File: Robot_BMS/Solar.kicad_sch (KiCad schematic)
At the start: 19 parts, among them J3 691137710002, U5 LM3488MM, U6 CSD18563Q5A

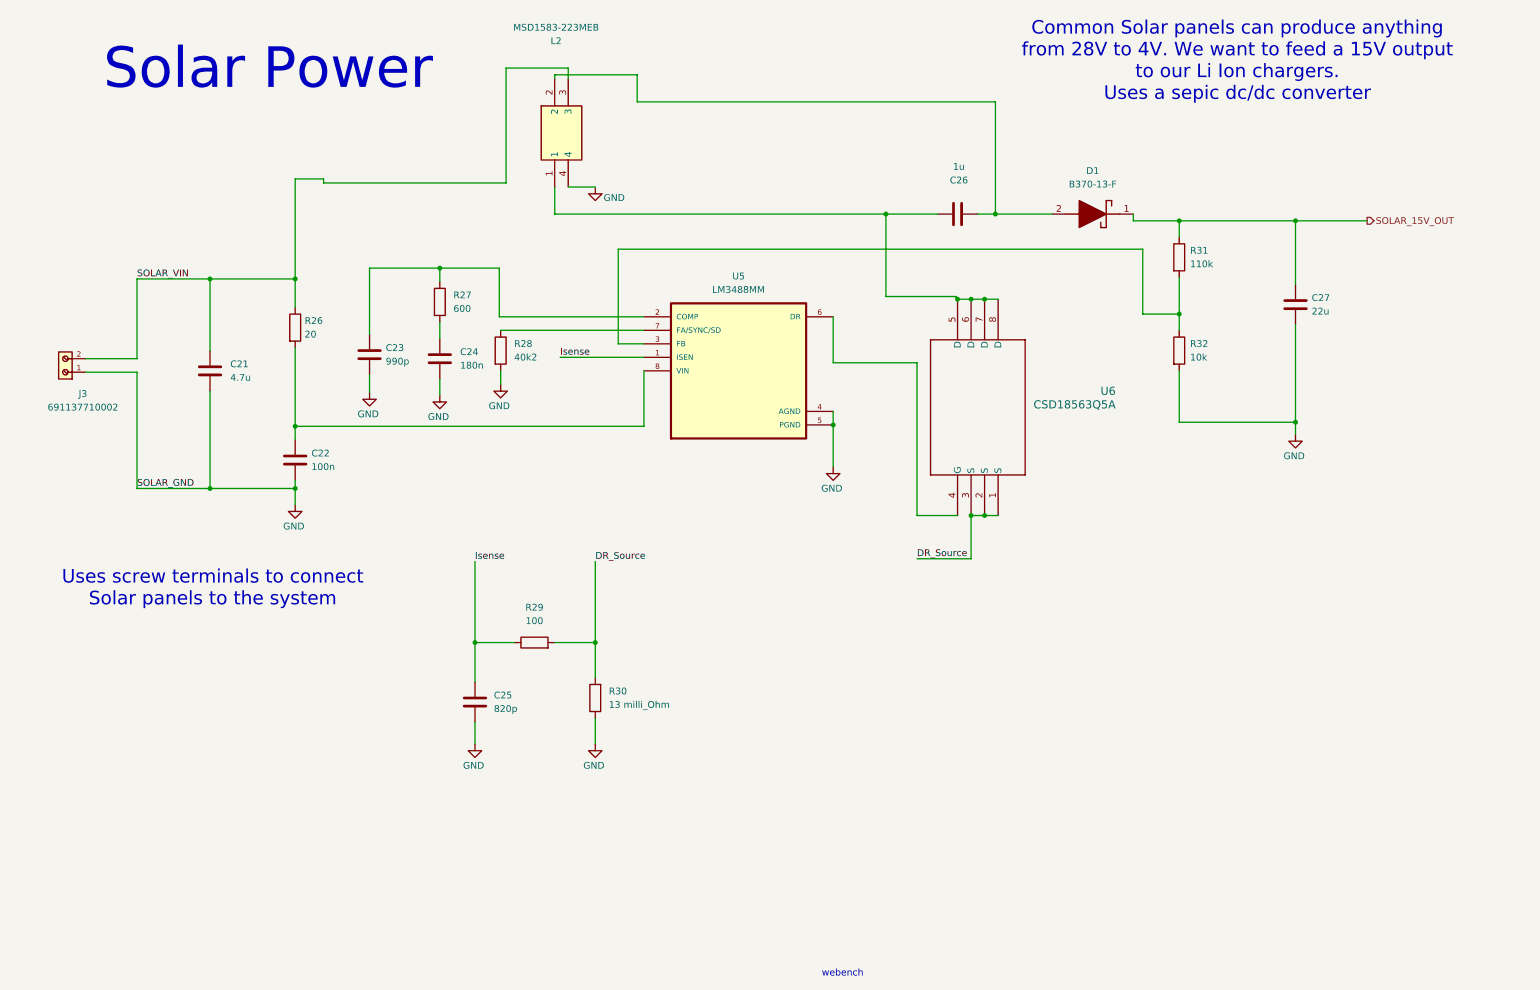
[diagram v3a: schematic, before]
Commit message: System drawing down on top schematic, will start inputting footprints
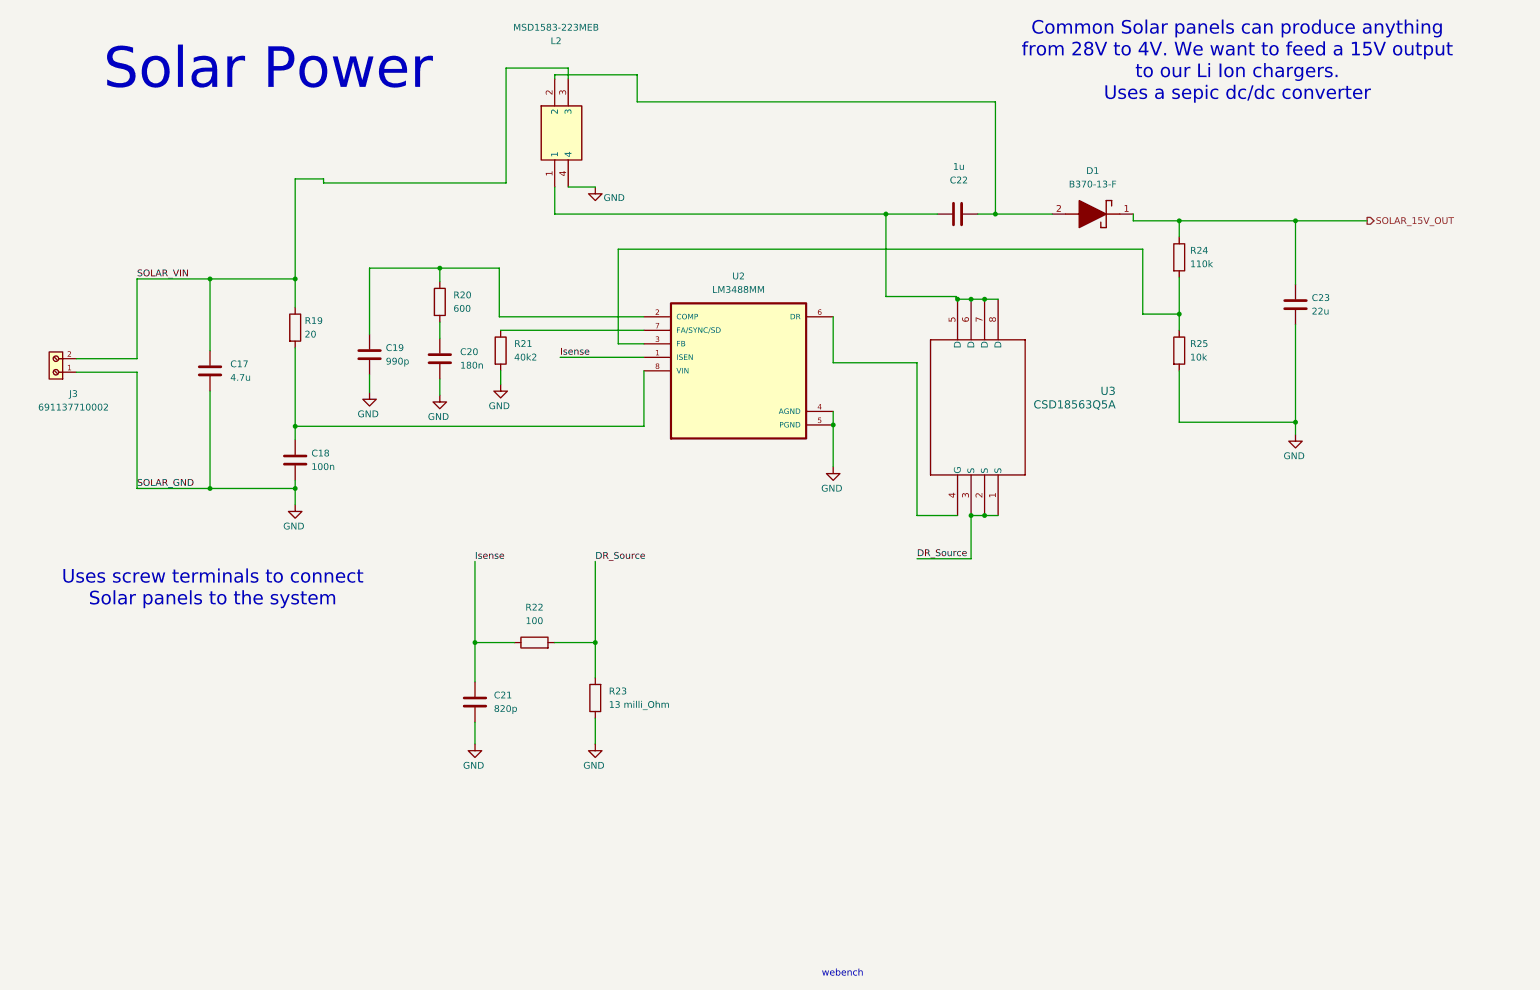
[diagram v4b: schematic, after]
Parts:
- renumbered C21 to C17, C22 to C18, C23 to C19, C24 to C20, C25 to C21, C26 to C22, C27 to C23, R26 to R19, R27 to R20, R28 to R21, R29 to R22, R30 to R23, R31 to R24, R32 to R25, U5 to U2, U6 to U3
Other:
- moved on the sheet: J3
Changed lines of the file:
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@@
 	(wire
 		(pts
-			(xy 21.082 78.994) (xy 30.734 78.994)
+			(xy 19.304 78.994) (xy 30.734 78.994)
 		)
 		(stroke
@@
 	(wire
 		(pts
-			(xy 21.082 81.534) (xy 30.734 81.534)
+			(xy 19.304 81.534) (xy 30.734 81.534)
 		)
 		(stroke
@@
 		(on_board yes)
 		(dnp no)
-		(property "Reference" "#PWR037"
+		(property "Reference" "#PWR030"
 			(at 60.452 112.776 0)
 			(effects
@@
 			(project "Robot_BMS"
 				(path "/72551b1c-3d40-4199-8911-e5b015f4abec/ff8c01d9-7d3c-4161-8f4f-7a8402a9daec"
-					(reference "#PWR037")
+					(reference "#PWR030")
 					(unit 1)
 				)
@@
 		(dnp no)
 		(fields_autoplaced yes)
-		(property "Reference" "U5"
+		(property "Reference" "U2"
 			(at 143.764 63.5 0)
 			(effects
@@
 			(project ""
 				(path "/72551b1c-3d40-4199-8911-e5b015f4abec/ff8c01d9-7d3c-4161-8f4f-7a8402a9daec"
-					(reference "U5")
+					(reference "U2")
 					(unit 1)
 				)
@@
 		(on_board yes)
 		(dnp no)
-		(property "Reference" "#PWR044"
+		(property "Reference" "#PWR037"
 			(at 161.544 105.664 0)
 			(effects
@@
 			(project "Robot_BMS"
 				(path "/72551b1c-3d40-4199-8911-e5b015f4abec/ff8c01d9-7d3c-4161-8f4f-7a8402a9daec"
-					(reference "#PWR044")
+					(reference "#PWR037")
 					(unit 1)
 				)
@@
 		(dnp no)
 		(fields_autoplaced yes)
-		(property "Reference" "C21"
+		(property "Reference" "C17"
 			(at 48.26 80.0099 0)
 			(effects
@@
 			(project ""
 				(path "/72551b1c-3d40-4199-8911-e5b015f4abec/ff8c01d9-7d3c-4161-8f4f-7a8402a9daec"
-					(reference "C21")
+					(reference "C17")
 					(unit 1)
 				)
@@
 		(on_board yes)
 		(dnp no)
-		(property "Reference" "U6"
+		(property "Reference" "U3"
 			(at 214.63 85.09 90)
 			(effects
@@
 			(project ""
 				(path "/72551b1c-3d40-4199-8911-e5b015f4abec/ff8c01d9-7d3c-4161-8f4f-7a8402a9daec"
-					(reference "U6")
+					(reference "U3")
 					(unit 1)
 				)
@@
 		(dnp no)
 		(fields_autoplaced yes)
-		(property "Reference" "R27"
+		(property "Reference" "R20"
 			(at 90.17 67.0559 0)
 			(effects
@@
 			(project "Robot_BMS"
 				(path "/72551b1c-3d40-4199-8911-e5b015f4abec/ff8c01d9-7d3c-4161-8f4f-7a8402a9daec"
-					(reference "R27")
+					(reference "R20")
 					(unit 1)
 				)
@@
 		(on_board yes)
 		(dnp no)
-		(property "Reference" "#PWR041"
+		(property "Reference" "#PWR034"
 			(at 99.06 90.17 0)
 			(effects
@@
 			(project "Robot_BMS"
 				(path "/72551b1c-3d40-4199-8911-e5b015f4abec/ff8c01d9-7d3c-4161-8f4f-7a8402a9daec"
-					(reference "#PWR041")
+					(reference "#PWR034")
 					(unit 1)
 				)
@@
 		(dnp no)
 		(fields_autoplaced yes)
-		(property "Reference" "R29"
+		(property "Reference" "R22"
 			(at 105.41 125.73 90)
 			(effects
@@
 			(project "Robot_BMS"
 				(path "/72551b1c-3d40-4199-8911-e5b015f4abec/ff8c01d9-7d3c-4161-8f4f-7a8402a9daec"
-					(reference "R29")
+					(reference "R22")
 					(unit 1)
 				)
@@
 		(dnp no)
 		(fields_autoplaced yes)
-		(property "Reference" "R30"
+		(property "Reference" "R23"
 			(at 119.38 141.4779 0)
 			(effects
@@
 			(project "Robot_BMS"
 				(path "/72551b1c-3d40-4199-8911-e5b015f4abec/ff8c01d9-7d3c-4161-8f4f-7a8402a9daec"
-					(reference "R30")
+					(reference "R23")
 					(unit 1)
 				)
@@
 		(dnp no)
 		(fields_autoplaced yes)
-		(property "Reference" "R28"
+		(property "Reference" "R21"
 			(at 101.6 76.1999 0)
 			(effects
@@
 			(project ""
 				(path "/72551b1c-3d40-4199-8911-e5b015f4abec/ff8c01d9-7d3c-4161-8f4f-7a8402a9daec"
-					(reference "R28")
+					(reference "R21")
 					(unit 1)
 				)
@@
 		(dnp no)
 		(fields_autoplaced yes)
-		(property "Reference" "C27"
+		(property "Reference" "C23"
 			(at 251.46 67.5639 0)
 			(effects
@@
 			(project "Robot_BMS"
 				(path "/72551b1c-3d40-4199-8911-e5b015f4abec/ff8c01d9-7d3c-4161-8f4f-7a8402a9daec"
-					(reference "C27")
+					(reference "C23")
 					(unit 1)
 				)
@@
 		(dnp no)
 		(fields_autoplaced yes)
-		(property "Reference" "R32"
+		(property "Reference" "R25"
 			(at 228.6 76.1999 0)
 			(effects
@@
 			(project "Robot_BMS"
 				(path "/72551b1c-3d40-4199-8911-e5b015f4abec/ff8c01d9-7d3c-4161-8f4f-7a8402a9daec"
-					(reference "R32")
+					(reference "R25")
 					(unit 1)
 				)
@@
 		(on_board yes)
 		(dnp no)
-		(property "Reference" "#PWR045"
+		(property "Reference" "#PWR038"
 			(at 248.412 99.568 0)
 			(effects
@@
 			(project "Robot_BMS"
 				(path "/72551b1c-3d40-4199-8911-e5b015f4abec/ff8c01d9-7d3c-4161-8f4f-7a8402a9daec"
-					(reference "#PWR045")
+					(reference "#PWR038")
 					(unit 1)
 				)
@@
 		(on_board yes)
 		(dnp no)
-		(property "Reference" "C26"
+		(property "Reference" "C22"
 			(at 185.166 45.466 90)
 			(effects
@@
 			(project "Robot_BMS"
 				(path "/72551b1c-3d40-4199-8911-e5b015f4abec/ff8c01d9-7d3c-4161-8f4f-7a8402a9daec"
-					(reference "C26")
+					(reference "C22")
 					(unit 1)
 				)
@@
 		(on_board yes)
 		(dnp no)
-		(property "Reference" "#PWR038"
+		(property "Reference" "#PWR031"
 			(at 74.422 91.694 0)
 			(effects
@@
 			(project "Robot_BMS"
 				(path "/72551b1c-3d40-4199-8911-e5b015f4abec/ff8c01d9-7d3c-4161-8f4f-7a8402a9daec"
-					(reference "#PWR038")
+					(reference "#PWR031")
 					(unit 1)
 				)
@@
 		(on_board yes)
 		(dnp no)
-		(property "Reference" "#PWR039"
+		(property "Reference" "#PWR032"
 			(at 87.63 92.202 0)
 			(effects
@@
 			(project "Robot_BMS"
 				(path "/72551b1c-3d40-4199-8911-e5b015f4abec/ff8c01d9-7d3c-4161-8f4f-7a8402a9daec"
-					(reference "#PWR039")
+					(reference "#PWR032")
 					(unit 1)
 				)
@@
 		(dnp no)
 		(fields_autoplaced yes)
-		(property "Reference" "R26"
+		(property "Reference" "R19"
 			(at 62.23 71.8819 0)
 			(effects
@@
 			(project ""
 				(path "/72551b1c-3d40-4199-8911-e5b015f4abec/ff8c01d9-7d3c-4161-8f4f-7a8402a9daec"
-					(reference "R26")
+					(reference "R19")
 					(unit 1)
 				)
@@
 	(symbol
 		(lib_id "691137710002-2 Terminal Connector:691137710002")
-		(at 16.002 78.994 90)
+		(at 14.224 78.994 90)
 		(unit 1)
 		(exclude_from_sim no)
@@
 		(dnp no)
 		(property "Reference" "J3"
-			(at 20.574 85.598 90)
+			(at 18.796 85.598 90)
 			(effects
 				(font
@@
 		)
 		(property "Value" "691137710002"
-			(at 20.574 88.138 90)
+			(at 18.796 88.138 90)
 			(effects
 				(font
@@
 		)
 		(property "Footprint" "691137710002:691137710002"
-			(at 16.002 78.994 0)
+			(at 14.224 78.994 0)
 			(effects
 				(font
@@
 		)
 		(property "Datasheet" ""
-			(at 16.002 78.994 0)
+			(at 14.224 78.994 0)
 			(effects
 				(font
@@
 		)
 		(property "Description" ""
-			(at 16.002 78.994 0)
+			(at 14.224 78.994 0)
 			(effects
 				(font
@@
 		(dnp no)
 		(fields_autoplaced yes)
-		(property "Reference" "C24"
+		(property "Reference" "C20"
 			(at 91.44 77.7239 0)
 			(effects
@@
 			(project "Robot_BMS"
 				(path "/72551b1c-3d40-4199-8911-e5b015f4abec/ff8c01d9-7d3c-4161-8f4f-7a8402a9daec"
-					(reference "C24")
+					(reference "C20")
 					(unit 1)
 				)
@@
 		(dnp no)
 		(fields_autoplaced yes)
-		(property "Reference" "C22"
+		(property "Reference" "C18"
 			(at 63.5 96.7739 0)
 			(effects
@@
 			(project "Robot_BMS"
 				(path "/72551b1c-3d40-4199-8911-e5b015f4abec/ff8c01d9-7d3c-4161-8f4f-7a8402a9daec"
-					(reference "C22")
+					(reference "C18")
 					(unit 1)
 				)
@@
 		(on_board yes)
 		(dnp no)
-		(property "Reference" "#PWR042"
+		(property "Reference" "#PWR035"
 			(at 116.84 53.086 0)
 			(effects
@@
 			(project "Robot_BMS"
 				(path "/72551b1c-3d40-4199-8911-e5b015f4abec/ff8c01d9-7d3c-4161-8f4f-7a8402a9daec"
-					(reference "#PWR042")
+					(reference "#PWR035")
 					(unit 1)
 				)
@@
 		(on_board yes)
 		(dnp no)
-		(property "Reference" "#PWR043"
+		(property "Reference" "#PWR036"
 			(at 116.84 157.734 0)
 			(effects
@@
 			(project "Robot_BMS"
 				(path "/72551b1c-3d40-4199-8911-e5b015f4abec/ff8c01d9-7d3c-4161-8f4f-7a8402a9daec"
-					(reference "#PWR043")
+					(reference "#PWR036")
 					(unit 1)
 				)
@@
 		(dnp no)
 		(fields_autoplaced yes)
-		(property "Reference" "C25"
+		(property "Reference" "C21"
 			(at 97.79 142.2399 0)
 			(effects
@@
 			(project "Robot_BMS"
 				(path "/72551b1c-3d40-4199-8911-e5b015f4abec/ff8c01d9-7d3c-4161-8f4f-7a8402a9daec"
-					(reference "C25")
+					(reference "C21")
 					(unit 1)
 				)
@@
 		(on_board yes)
 		(dnp no)
-		(property "Reference" "#PWR040"
+		(property "Reference" "#PWR033"
 			(at 94.234 157.734 0)
 			(effects
@@
 			(project "Robot_BMS"
 				(path "/72551b1c-3d40-4199-8911-e5b015f4abec/ff8c01d9-7d3c-4161-8f4f-7a8402a9daec"
-					(reference "#PWR040")
+					(reference "#PWR033")
 					(unit 1)
 				)
@@
 		(dnp no)
 		(fields_autoplaced yes)
-		(property "Reference" "C23"
+		(property "Reference" "C19"
 			(at 77.47 76.9619 0)
 			(effects
@@
 			(project "Robot_BMS"
 				(path "/72551b1c-3d40-4199-8911-e5b015f4abec/ff8c01d9-7d3c-4161-8f4f-7a8402a9daec"
-					(reference "C23")
+					(reference "C19")
 					(unit 1)
 				)
@@
 		(dnp no)
 		(fields_autoplaced yes)
-		(property "Reference" "R31"
+		(property "Reference" "R24"
 			(at 228.6 58.6739 0)
 			(effects
@@
 			(project "Robot_BMS"
 				(path "/72551b1c-3d40-4199-8911-e5b015f4abec/ff8c01d9-7d3c-4161-8f4f-7a8402a9daec"
-					(reference "R31")
-					(unit 1)
-				)
+					(reference "R24")
+					(unit 1)
+				)

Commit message: adding footprints and actual passive components
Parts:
- D1: footprint DIOM7959X250N -> RobotBMS:DIOM7959X250N
- J4: renamed from J3; footprint 691137710002:691137710002 -> RobotBMS:691137710002
- L2: footprint MSD1583223MEB -> RobotBMS:MSD1583223MEB
- U2: footprint LM3488MM:SOP65P490X110-8N -> RobotBMS:SOP65P490X110-8N
- U3: footprint DQJ8 -> RobotBMS:DQJ8
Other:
- note added: "All standard Passive componenets are 0603 imperial"
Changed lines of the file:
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@@
+		)
+	)
+	(text "All standard Passive\ncomponenets are 0603 imperial"
+		(exclude_from_sim no)
+		(at 223.012 173.482 0)
+		(effects
+			(font
+				(size 2.54 2.54)
+			)
 		)
 	)
@@
 			)
 		)
-		(property "Footprint" "LM3488MM:SOP65P490X110-8N"
+		(property "Footprint" "RobotBMS:SOP65P490X110-8N"
 			(at 143.764 81.28 0)
 			(effects
@@
 			)
 		)
-		(property "Footprint" "DQJ8"
+		(property "Footprint" "RobotBMS:DQJ8"
 			(at 192.532 108.458 0)
 			(effects
@@
 			)
 		)
-		(property "Footprint" "DIOM7959X250N"
+		(property "Footprint" "RobotBMS:DIOM7959X250N"
 			(at 207.772 -41.834 0)
 			(effects
@@
 		(on_board yes)
 		(dnp no)
-		(property "Reference" "J3"
+		(property "Reference" "J4"
 			(at 18.796 85.598 90)
 			(effects
@@
 			)
 		)
-		(property "Footprint" "691137710002:691137710002"
+		(property "Footprint" "RobotBMS:691137710002"
 			(at 14.224 78.994 0)
 			(effects
@@
 			(project ""
 				(path "/72551b1c-3d40-4199-8911-e5b015f4abec/ff8c01d9-7d3c-4161-8f4f-7a8402a9daec"
-					(reference "J3")
+					(reference "J4")
 					(unit 1)
 				)
@@
 			)
 		)
-		(property "Footprint" "MSD1583223MEB"
+		(property "Footprint" "RobotBMS:MSD1583223MEB"
 			(at 204.14 42.926 0)
 			(effects

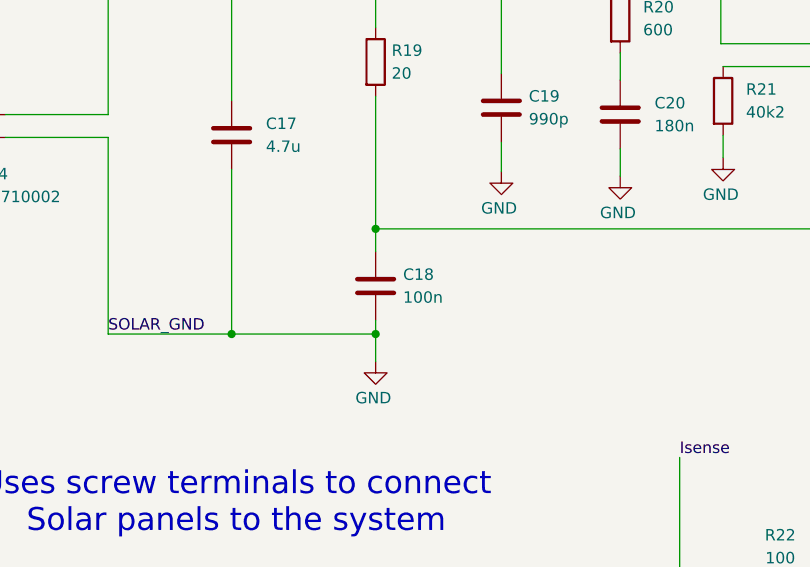
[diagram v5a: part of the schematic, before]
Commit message: adding footprints and actual passive components pt.2
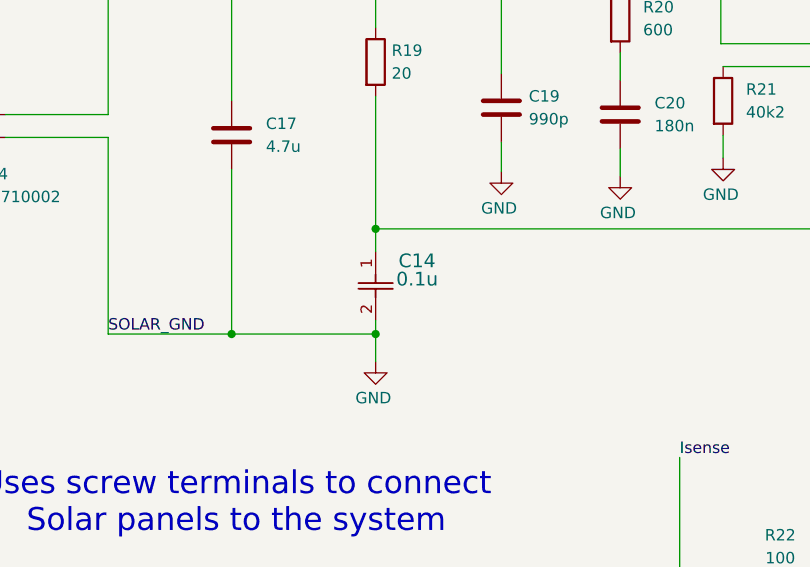
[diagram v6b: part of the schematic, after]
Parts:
- removed C18: 100n, symbol Device:C
- added C14: 0.1u, CAPC17595_87N_KEM, symbol C0603C104K5RACAUTO:C0603C104K5RACAUTO
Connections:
- net GND: now also C14.2
- net at R19.2, U2.8 (VIN): now also C14.1
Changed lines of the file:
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@@
-	)
-	(symbol
-		(lib_id "Device:C")
-		(at 60.452 98.044 0)
-		(unit 1)
-		(exclude_from_sim no)
-		(in_bom yes)
-		(on_board yes)
-		(dnp no)
-		(fields_autoplaced yes)
-		(property "Reference" "C18"
-			(at 63.5 96.7739 0)
-			(effects
-				(font
-					(size 1.27 1.27)
-				)
-				(justify left)
-			)
-		)
-		(property "Value" "100n"
-			(at 63.5 99.3139 0)
-			(effects
-				(font
-					(size 1.27 1.27)
-				)
-				(justify left)
-			)
-		)
-		(property "Footprint" ""
-			(at 61.4172 101.854 0)
-			(effects
-				(font
-					(size 1.27 1.27)
-				)
-				(hide yes)
-			)
-		)
-		(property "Datasheet" "~"
-			(at 60.452 98.044 0)
-			(effects
-				(font
-					(size 1.27 1.27)
-				)
-				(hide yes)
-			)
-		)
-		(property "Description" "Unpolarized capacitor"
-			(at 60.452 98.044 0)
-			(effects
-				(font
-					(size 1.27 1.27)
-				)
-				(hide yes)
-			)
-		)
-		(pin "1"
-		)
-		(pin "2"
-		)
-		(instances
-			(project "Robot_BMS"
-				(path "/72551b1c-3d40-4199-8911-e5b015f4abec/ff8c01d9-7d3c-4161-8f4f-7a8402a9daec"
-					(reference "C18")
-					(unit 1)
-				)
-			)
-		)
 	)
 	(symbol
@@
 					(unit 1)
 				)
+			)
+		)
+	)
+	(symbol
+		(lib_id "C0603C104K5RACAUTO:C0603C104K5RACAUTO")
+		(at 60.452 94.234 270)
+		(unit 1)
+		(exclude_from_sim no)
+		(in_bom yes)
+		(on_board yes)
+		(dnp no)
+		(property "Reference" "C14"
+			(at 62.992 95.25 90)
+			(effects
+				(font
+					(size 1.524 1.524)
+				)
+				(justify left)
+			)
+		)
+		(property "Value" "0.1u"
+			(at 62.738 97.282 90)
+			(effects
+				(font
+					(size 1.524 1.524)
+				)
+				(justify left)
+			)
+		)
+		(property "Footprint" "CAPC17595_87N_KEM"
+			(at 60.452 94.234 0)
+			(effects
+				(font
+					(size 1.27 1.27)
+					(italic yes)
+				)
+				(hide yes)
+			)
+		)
+		(property "Datasheet" "C0603C104K5RACAUTO"
+			(at 60.452 94.234 0)
+			(effects
+				(font
+					(size 1.27 1.27)
+					(italic yes)
+				)
+				(hide yes)
+			)
+		)
+		(property "Description" "C0603C104K5RACAUTO"
+			(at 60.452 94.234 0)
+			(effects
+				(font
+					(size 1.27 1.27)
+				)
+				(hide yes)
+			)
+		)
+		(pin "2"
+		)
+		(pin "1"
+		)
+		(instances
+			(project "Robot_BMS"
+				(path "/72551b1c-3d40-4199-8911-e5b015f4abec/ff8c01d9-7d3c-4161-8f4f-7a8402a9daec"
+					(reference "C14")
+					(unit 1)
+				)
